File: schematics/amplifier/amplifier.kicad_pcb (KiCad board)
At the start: 2 copper layers, 41 parts, among them J1 Conn_01x01_Male, J2 Conn_01x01_Male, J3 FC68131, J4 Jack-DC, J5 Screw_Terminal_01x02, Q1 BC547, Q2 BC557, Q3 BC547, Q4 BC337, Q5 BC327

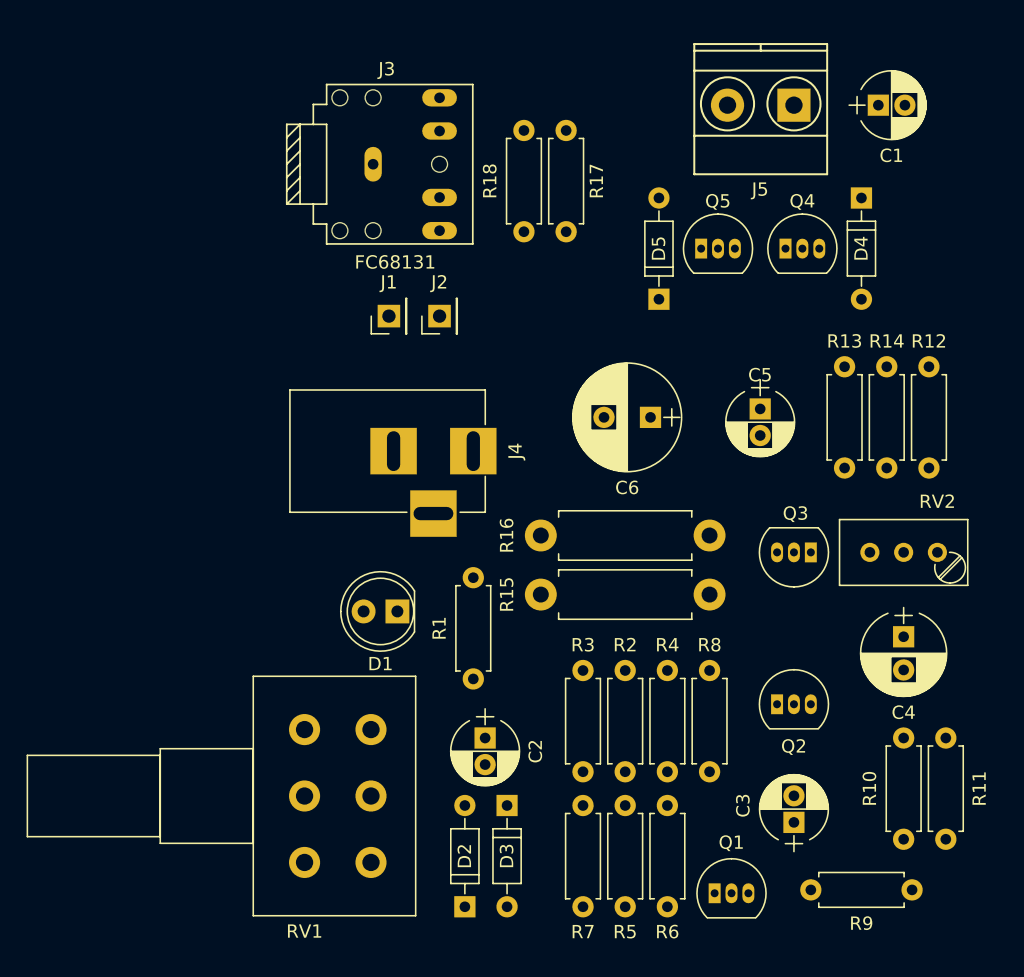
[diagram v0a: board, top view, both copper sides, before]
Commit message: Rename amplifier circuit project files
The amplifier circuit's project has been renamed from
'FirstAudioAmplifier' to 'amplifier'.
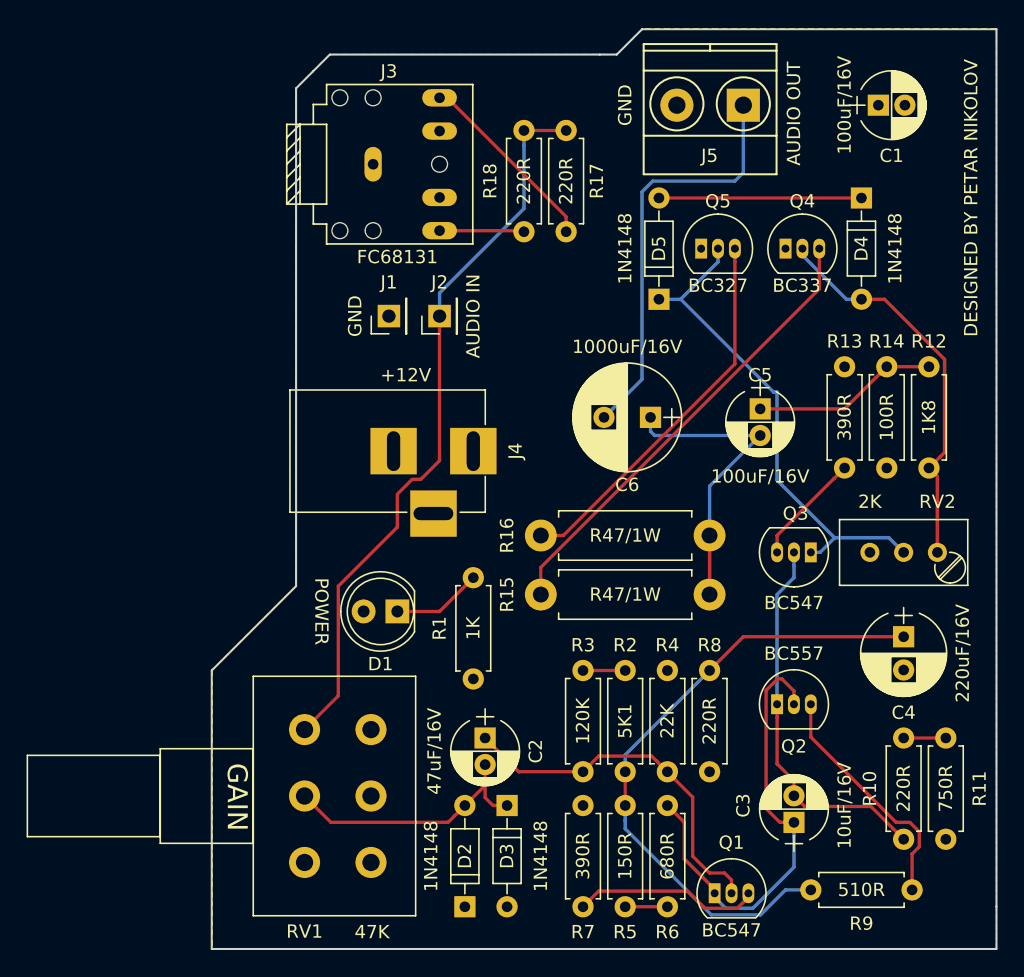
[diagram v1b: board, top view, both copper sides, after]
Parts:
- moved J5 3.81 mm to (128.9, 66.7)
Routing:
- net /AUDIO_IN: track 0.00 -> 55.5 mm
- net Net-(C4-Pad1): track 0.00 -> 47.6 mm
- net Net-(D5-Pad1): track 0.00 -> 37.4 mm
- net Net-(Q4-Pad3): track 0.00 -> 34.7 mm
- net Net-(C3-Pad1): track 0.00 -> 34.6 mm
- net /AUDIO_OUT: track 0.00 -> 31.5 mm
- net Net-(D4-Pad2): track 0.00 -> 29.7 mm
- net Net-(C3-Pad2): track 0.00 -> 29.0 mm
- net Net-(Q5-Pad3): track 0.00 -> 28.6 mm
- net Net-(C2-Pad1): track 0.00 -> 27.5 mm
- net Net-(C5-Pad2): track 0.00 -> 23.0 mm
- net Net-(C2-Pad2): track 0.00 -> 19.9 mm
- net Net-(Q2-Pad3): track 0.00 -> 18.2 mm
- net Net-(D4-Pad1): track 0.00 -> 15.2 mm
- net Net-(J3-Pad5): track 0.00 -> 14.4 mm
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- added copper zone on F.Cu, net +12V
- added copper zone on B.Cu, net GND
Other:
- board outline added: 59.1 x 69.2 mm
- net class Default: clearance 0.2 -> 0.25
- rule trace_clearance: 0.2 -> 0.25
- board text added: "+12V"
- board text added: "AUDIO IN"
- board text added: "AUDIO OUT"
- board text added: "DESIGNED BY PETAR NIKOLOV"
- board text added: "GAIN"
- board text added: "GND"
- board text added: "POWER"
